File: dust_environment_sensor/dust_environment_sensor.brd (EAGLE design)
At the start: 60 x 34 mm, 4 parts, among them U1 LTP5901, U2 LIS3DH, U3 SI7005, U4 TSL2560

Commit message: Battery holder
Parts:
- added J1: (no value), Cool_Electricity:BX0036
- moved U1 14.1 mm to (30.5, 15.5), turned to 180 degrees
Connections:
- net GND: now also J1.NEG
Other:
- board size 60 x 34 mm -> 60 x 35 mm
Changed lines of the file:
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@@
 <board>
 <plain>
-<wire x1="0" y1="0" x2="60" y2="0" width="0" layer="20"/>
-<wire x1="60" y1="0" x2="60" y2="34" width="0" layer="20"/>
+<wire x1="0" y1="-1" x2="60" y2="-1" width="0" layer="20"/>
+<wire x1="60" y1="-1" x2="60" y2="34" width="0" layer="20"/>
 <wire x1="60" y1="34" x2="0" y2="34" width="0" layer="20"/>
-<wire x1="0" y1="34" x2="0" y2="0" width="0" layer="20"/>
+<wire x1="0" y1="34" x2="0" y2="-1" width="0" layer="20"/>
 </plain>
 <attributes>
@@
 </autorouter>
 <elements>
-<element name="U1" library="Cool_Electricity" package="LTP5901_MODULE" value="LTP5901" x="16.51" y="17.51" rot="R90"/>
+<element name="U1" library="Cool_Electricity" package="LTP5901_MODULE" value="LTP5901" x="30.49" y="15.51" rot="R180"/>
 <element name="U2" library="Cool_Electricity" package="LGA16_ST" value="LIS3DH" x="43.18" y="19.05"/>
 <element name="U3" library="Cool_Electricity" package="QFN24_SILICON_LABS" value="SI7005" x="41.91" y="27.94" rot="R90"/>
 <element name="U4" library="Cool_Electricity" package="CL6_TAOS" value="TSL2560" x="45.72" y="11.43"/>
+<element name="J1" library="Cool_Electricity" package="BX0036" value="" x="30" y="17" rot="MR0"/>
 </elements>
 <signals>
@@
 <contactref element="U2" pad="12"/>
 <contactref element="U2" pad="10"/>
-<wire x1="22.01" y1="5.51" x2="32.01" y2="5.51" width="0" layer="19" extent="1-1"/>
-<wire x1="13.01" y1="5.51" x2="22.01" y2="5.51" width="0" layer="19" extent="1-1"/>
-<wire x1="3.01" y1="5.51" x2="13.01" y2="5.51" width="0" layer="19" extent="1-1"/>
-<wire x1="33.01" y1="21.51" x2="32.01" y2="5.51" width="0" layer="19" extent="1-1"/>
-<wire x1="32.01" y1="29.51" x2="33.01" y2="21.51" width="0" layer="19" extent="1-1"/>
-<wire x1="27.01" y1="29.51" x2="32.01" y2="29.51" width="0" layer="19" extent="1-1"/>
-<wire x1="13.01" y1="29.51" x2="27.01" y2="29.51" width="0" layer="19" extent="1-1"/>
-<wire x1="3.01" y1="29.51" x2="13.01" y2="29.51" width="0" layer="19" extent="1-1"/>
-<wire x1="44.035" y1="28.69" x2="3.01" y2="29.51" width="0" layer="19" extent="1-1"/>
+<contactref element="J1" pad="NEG"/>
 <wire x1="44.035" y1="27.19" x2="44.035" y2="28.69" width="0" layer="19" extent="1-1"/>
 <wire x1="41.91" y1="27.94" x2="44.035" y2="28.69" width="0" layer="19" extent="1-1"/>
+<wire x1="40.66" y1="25.815" x2="41.91" y2="27.94" width="0" layer="19" extent="1-1"/>
 <wire x1="39.785" y1="29.19" x2="41.91" y2="27.94" width="0" layer="19" extent="1-1"/>
-<wire x1="40.66" y1="25.815" x2="41.91" y2="27.94" width="0" layer="19" extent="1-1"/>
 <wire x1="44.73" y1="19.55" x2="40.66" y2="25.815" width="0" layer="19" extent="1-1"/>
 <wire x1="44.73" y1="18.55" x2="44.73" y2="19.55" width="0" layer="19" extent="1-1"/>
 <wire x1="41.63" y1="18.05" x2="44.73" y2="18.55" width="0" layer="19" extent="1-1"/>
+<wire x1="18.49" y1="31.01" x2="39.785" y2="29.19" width="0" layer="19" extent="1-1"/>
+<wire x1="18.49" y1="26.01" x2="18.49" y2="31.01" width="0" layer="19" extent="1-1"/>
+<wire x1="26.49" y1="32.01" x2="18.49" y2="31.01" width="0" layer="19" extent="1-1"/>
+<wire x1="18.49" y1="12.01" x2="18.49" y2="26.01" width="0" layer="19" extent="1-1"/>
+<wire x1="18.49" y1="2.01" x2="18.49" y2="12.01" width="0" layer="19" extent="1-1"/>
+<wire x1="42.49" y1="31.01" x2="41.63" y2="18.05" width="0" layer="19" extent="1-1"/>
+<wire x1="42.49" y1="21.01" x2="42.49" y2="31.01" width="0" layer="19" extent="1-1"/>
+<wire x1="42.49" y1="12.01" x2="42.49" y2="21.01" width="0" layer="19" extent="1-1"/>
+<wire x1="42.49" y1="2.01" x2="42.49" y2="12.01" width="0" layer="19" extent="1-1"/>
+<wire x1="2.2" y1="17" x2="42.49" y2="31.01" width="0" layer="19" extent="1-1"/>
 </signal>
 </signals>

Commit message: more work on dust sensor
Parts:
- added C1, C3, C5: 100n, rcl:C0603
- added C2: 10u, rcl:C0603
- added C31, C32: 22p, SparkFun:0603
- added C33, C34, C41: .1u, SparkFun:0603
- added C4: 100u, rcl:C0603
- added C6: (no value), rcl:C0603
- added C7: 4.7u, rcl:C0603
- added JP1: (no value), custom:1X06
- added JP2: AVR_SPI_PRG_6NS, SparkFun:2X3-NS
- added R1, R2: 2.2k, resistor:R0603
- added R46: 10k, SparkFun:0603
- added U5: ATMEGA168, SparkFun:TQFP32-08
- added X1: 32.768KHz, WSNlib:ABS07
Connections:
- new net 5V: C33.2, C34.2, JP1.3, JP2.2, R46.2, U5.18, U5.4, U5.6
- new net ACCEL_INT1: U2.11
- new net ACCEL_INT2: U2.9
- new net ATMEGA_TO_MOTE: JP1.5, U1.59, U5.31
- new net HUMID_#CS: U3.15
- new net I2C_SCL: R1.1, U2.4, U3.3, U4.4, U5.28
- new net I2C_SDA: R2.1, U2.6, U3.4, U4.5, U5.27
- new net LIGHT_INT: U4.6
- new net MISO: JP2.1, U5.16
- new net MOSI: JP2.4, U5.15
- new net MOTE_TO_ATMEGA: JP1.4, U1.62, U5.30
- new net N$1: C7.1, U3.10
- new net N$2: C31.1, U5.7, X1.2
- new net N$4: C32.1, U5.8, X1.1
- new net RST: C41.1, JP2.5, R46.1, U5.29
- new net RTS#: C41.2, JP1.6
- new net SCLK: JP2.3, U5.17
- new net VCC: C1.1, C2.1, C3.1, C4.1, C5.1, C6.1, J1.POS, R1.2, R2.2, U1.55, U2.14, U2.7, U2.8, U3.9, U4.1
- net GND: now also C1.2, C2.2, C3.2, C31.2, C32.2, C33.1, C34.1, C4.2, C5.2, C6.2, C7.2, JP1.1, JP1.2, JP2.6, U4.2, U5.21, U5.3, U5.5

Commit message: BOM done
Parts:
- added JP3: .1" header, con-lstb:MA06-2
- added LED1: RED, led:CHIPLED_0805
- added R3: 15, resistor:R0603
- added R4: 120, SparkFun:0603
- added STANDOFF1, STANDOFF2, STANDOFF3, STANDOFF4: STAND-OFF, SparkFun-Electromechanical:STAND-OFF
- C4: device rcl:C0603 -> SparkFun-Capacitors:EIA3216-KIT
- C6: value (none) -> 100n
- J1: value (none) -> 3.6V Lithium C cell
- JP1: value (none) -> 87758-1016; device custom:1X06 -> con-molex:87758-1016
- U5: value ATMEGA168 -> ATMEGA328P
- moved JP2 156.6 mm to (50.0, 60.0), flipped to the bottom, turned to 270 degrees
- moved JP1 155.0 mm to (27.0, 54.0), turned to 180 degrees
- moved C41 146.1 mm to (32.0, 66.0), turned to 90 degrees
- moved R46 143.9 mm to (29.0, 65.0), turned to 180 degrees
- moved C34 141.8 mm to (42.0, 65.0)
- moved X1 139.2 mm to (44.0, 51.0), turned to 180 degrees
- moved C33 128.8 mm to (41.0, 51.0), turned to 90 degrees
- moved C31 128.7 mm to (43.0, 48.0), turned to 270 degrees
- moved C32 128.4 mm to (46.0, 48.0), turned to 270 degrees
- moved U5 118.3 mm to (41.0, 58.0), turned to 90 degrees
- moved R2 111.4 mm to (53.0, 53.0), turned to 90 degrees
- moved R1 106.9 mm to (50.9, 53.0), turned to 90 degrees
- moved C2 89.2 mm to (62.0, 49.0)
- moved C5 85.0 mm to (59.0, 34.0)
- moved C1 84.3 mm to (58.0, 50.0)
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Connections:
- removed net 5V: C33.2, C34.2, JP1.3, JP2.2, R46.2, U5.18, U5.4, U5.6
- removed net ATMEGA_TO_MOTE: JP1.5, U1.59, U5.31
- removed net HUMID_#CS: U3.15
- removed net MOTE_TO_ATMEGA: JP1.4, U1.62, U5.30
- new net ATMEGA_RX: JP3.7, U5.30
- new net ATMEGA_TX: JP3.9, U5.31
- new net FLASH_P_ENN: JP1.2, U1.51
- new net HUMID_VCC: R3.2, U5.25
- new net IPCS_MISO: JP1.5, U1.33
- new net IPCS_MOSI: JP1.4, U1.35
- new net IPCS_SCK: JP1.3, U1.36
- new net IPCS_SSN: JP1.1, U1.39
- new net LED1: R4.2, U5.26
- new net MOTE_API_RX: JP3.10, U1.59
- new net MOTE_API_TX: JP3.8, U1.62
- new net MOTE_CLI_RX: JP1.10, U1.32
- new net MOTE_CLI_TX: JP1.9, U1.31
- new net MOTE_RADIO_INHIBIT: U1.64, U5.12
- new net MOTE_RESETN: JP1.6, U1.15, U5.11
- new net MOTE_RX_CTSN: U1.58, U5.10
- new net MOTE_RX_RTSN: U1.57, U5.9
- new net MOTE_SLEEPN: U1.27, U5.13
- new net MOTE_TIMEN: U1.63, U5.14
- new net MOTE_TX_CTSN: U1.61, U5.2
- new net MOTE_TX_RTSN: U1.60, U5.1
- new net N$3: C5.1, R3.1, U3.9
- new net N$5: LED1.A, R4.1
- new net VBATT: C4.A, J1.POS, JP3.4
- net ACCEL_INT1: now also U5.32
- net ACCEL_INT2: now also U5.23
- net GND: now also C4.C, JP1.8, JP3.1, JP3.3, LED1.C, U3.15, U5.19, U5.22; no longer C4.2, JP1.1, JP1.2
- net LIGHT_INT: now also U5.24
- net RTS#: now also JP3.11; no longer JP1.6
- net VCC: now also C33.2, C34.2, JP1.7, JP2.2, JP3.6, R46.2, U5.18, U5.4, U5.6; no longer C4.1, C5.1, J1.POS, U3.9
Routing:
- net GND: track 0.00 -> 272.6 mm, vias 0 -> 1
- net VCC: track 0.00 -> 192.7 mm, vias 0 -> 2
- net MOTE_RADIO_INHIBIT: track 0.00 -> 95.4 mm, vias 0 -> 2
- net MOTE_TIMEN: track 0.00 -> 89.9 mm, vias 0 -> 2
- net I2C_SDA: track 0.00 -> 69.6 mm, vias 0 -> 5
- net MOTE_API_TX: track 0.00 -> 68.1 mm, vias 0 -> 1
- net HUMID_VCC: track 0.00 -> 67.0 mm, vias 0 -> 2
- net MOTE_RESETN: track 0.00 -> 62.2 mm, vias 0 -> 2
- net FLASH_P_ENN: track 0.00 -> 59.5 mm
- net LIGHT_INT: track 0.00 -> 55.6 mm, vias 0 -> 2
- net MOTE_API_RX: track 0.00 -> 55.0 mm, vias 0 -> 2
- net I2C_SCL: track 0.00 -> 52.0 mm, vias 0 -> 5
- net MOTE_RX_RTSN: track 0.00 -> 50.6 mm, vias 0 -> 4
- net MOTE_RX_CTSN: track 0.00 -> 47.5 mm, vias 0 -> 4
- net MOTE_TX_CTSN: track 0.00 -> 44.2 mm, vias 0 -> 2
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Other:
- board size 60 x 35 mm -> 70.8 x 68.7 mm

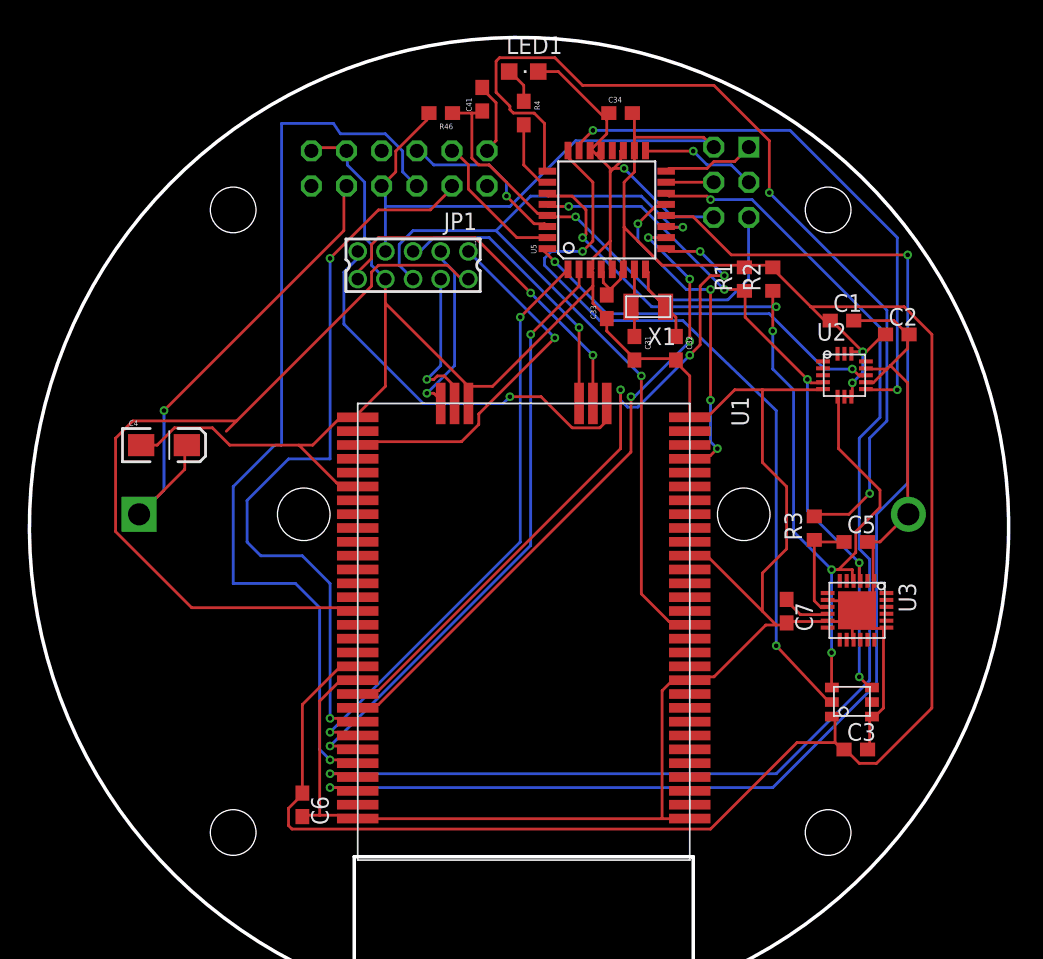
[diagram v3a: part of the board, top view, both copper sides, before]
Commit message: Added new version of power strip
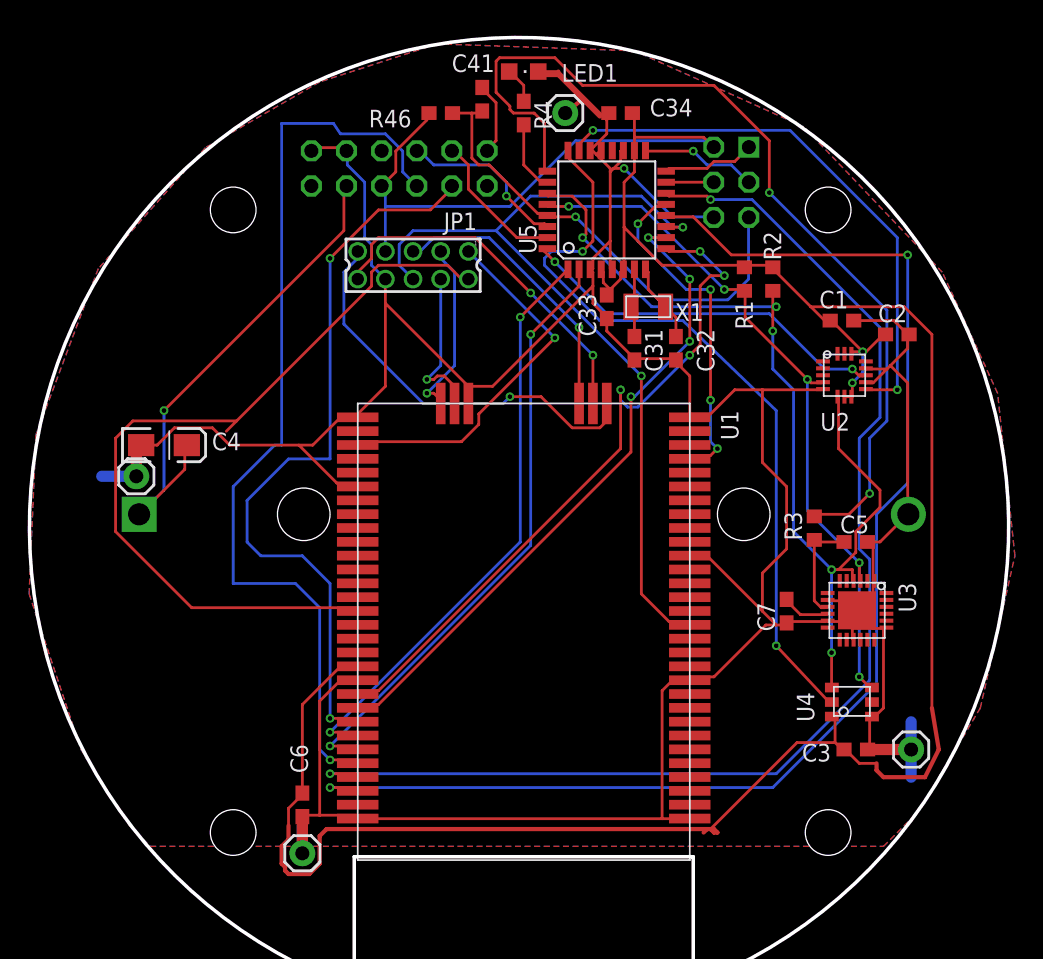
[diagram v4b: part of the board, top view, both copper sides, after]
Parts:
- added JP4, JP5, JP6, JP7: M01PTH, SparkFun-Connectors:1X01
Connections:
- net GND: now also JP4.1, JP5.1, JP6.1, JP7.1
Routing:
- net GND: track 272.6 -> 296.7 mm
- net VCC: track 192.7 -> 204.4 mm
- added copper zone on layer 16, net GND
- added copper zone on layer 1, net VCC
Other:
- board text added: "NEGATIVE"
- board text added: "POSITIVE"
- board text added: "U4"

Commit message: Latest Powerstrip changes
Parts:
- removed C31, C32: 22p, SparkFun:0603
- removed C33, C34, C41: .1u, SparkFun:0603
- removed JP2: AVR_SPI_PRG_6NS, SparkFun:2X3-NS
- removed JP3: .1" header, con-lstb:MA06-2
- removed LED1: RED, led:CHIPLED_0805
- removed R46: 10k, SparkFun:0603
- removed X1: 32.768KHz, WSNlib:ABS07
- added C10, C13, C15, C8, C9: 100n, rcl:C0603
- added C11, C12: TODO, rcl:C0603
- added C14: 10u, rcl:C0603
- added IC2: ATMEGA644A, atmel:TQFP44
- added J2: EXP, SparkFun-Connectors:2X3
- added J3: XBEE_1-10SMT, Cool_Electricity:XBEE_1-10_SMT
- added J4: XBEE_11-20SMT, Cool_Electricity:XBEE_11-20_SMT
- added JP8: (no value), custom:1X06
- added JP9: JTAG, SparkFun-Connectors:AVR_ICSP
- added LED2, LED3: (no value), led:CHIPLED_0805
- added R5: 0R, resistor:R0603
- added U6: L3GD20, Cool_Electricity:LGA16_4X4_ST
- added X2: 32.768KHz, WSNlib:ABS07
- R4: value 120 -> 10k; device SparkFun:0603 -> resistor:R0603
- U5: value ATMEGA328P -> AMN41121; device SparkFun:TQFP32-08 -> Cool_Electricity:AMN41121
- moved JP7 56.1 mm to (9.00, 17.0)
- moved C1 49.0 mm to (12.9, 30.9), turned to 270 degrees
- moved C6 47.1 mm to (64.0, 29.0)
- moved R4 45.2 mm to (9.75, 27.5)
- moved U5 19.2 mm to (22.0, 61.0), turned to 0 degrees
- moved JP6 8.00 mm to (7.00, 46.8)
- moved JP1 7.21 mm to (23.0, 48.0)
- moved C5 5.10 mm to (54.0, 33.0), turned to 90 degrees
- moved JP5 3.57 mm to (18.7, 7.94)
- moved C4 1.00 mm to (9.00, 42.0)
- moved R3 0.10 mm to (56.1, 35.0)
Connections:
- removed net ATMEGA_RX: JP3.7, U5.30
- removed net ATMEGA_TX: JP3.9, U5.31
- removed net MISO: JP2.1, U5.16
- removed net MOSI: JP2.4, U5.15
- removed net N$4: C32.1, U5.8, X1.1
- removed net N$5: LED1.A, R4.1
- removed net SCLK: JP2.3, U5.17
- new net ATMEGA_TO_FTDI: IC2.10, JP8.5
- new net EXP_CSN: IC2.44, J2.5
- new net EXP_MISO: IC2.2, J2.1
- new net EXP_MOSI: IC2.1, J2.4
- new net EXP_SCK: IC2.3, J2.3
- new net FTDI_TO_ATMEGA: IC2.9, JP8.4
- new net GYRO_INT2: IC2.43, U6.6
- new net LED2: IC2.13, LED3.A
- new net N$6: C11.1, IC2.25, X2.2
- new net N$7: C12.1, IC2.26, X2.1
- new net PIR_OUT: IC2.16, U5.OUT
- new net PIR_VCC: IC2.30, U5.VDD
- new net TCK: IC2.21, JP9.1
- new net TDI: IC2.24, JP9.9
- new net TDO: IC2.23, JP9.3
- new net TMS: IC2.22, JP9.5
- net ACCEL_INT1: now also IC2.37; no longer U5.32
- net ACCEL_INT2: now also IC2.36; no longer U5.23
- net GND: now also C11.2, C12.2, C13.2, C14.2, C15.2, C8.1, C9.1, IC2.18, IC2.28, IC2.39, IC2.6, J2.6, J3.10, JP8.1, JP8.2, JP9.10, JP9.2, LED2.C, LED3.C, U5.GND, U6.10, U6.11, U6.12, U6.13, U6.8, U6.9; no longer C31.2, C32.2, C33.1, C34.1, JP2.6, JP3.1, JP3.3, LED1.C, U5.19, U5.21, U5.22, U5.3, U5.5
- net HUMID_VCC: now also IC2.35; no longer U5.25
- net I2C_SCL: now also IC2.19, U6.2; no longer U5.28
- net I2C_SDA: now also IC2.20, U6.3; no longer U5.27
- net LED1: now also IC2.14, LED2.A; no longer R4.2, U5.26
- net LIGHT_INT: now also IC2.31; no longer U5.24
- net MOTE_API_RX: now also IC2.12, J3.3; no longer JP3.10
- net MOTE_API_TX: now also IC2.11, J3.2; no longer JP3.8
- net MOTE_RADIO_INHIBIT: now also IC2.32; no longer U5.12
- net MOTE_RESETN: now also J3.5; no longer U5.11
- net MOTE_RX_CTSN: now also IC2.40; no longer U5.10
- net MOTE_RX_RTSN: now also IC2.15, J4.16; no longer U5.9
- net MOTE_SLEEPN: now also IC2.33, J3.9; no longer U5.13
- net MOTE_TIMEN: now also IC2.34; no longer U5.14
- net MOTE_TX_CTSN: now also IC2.41; no longer U5.2
- net MOTE_TX_RTSN: now also IC2.42; no longer U5.1
- net N$2: now also C15.1, U6.14; no longer C31.1, U5.7, X1.2
- net RST: now also C10.1, IC2.4, JP9.6, R4.1; no longer C41.1, JP2.5, R46.1, U5.29
- net RTS#: now also C10.2, JP8.6; no longer C41.2, JP3.11
- net VBATT: now also R5.2; no longer JP3.4
- net VCC: now also C13.1, C14.1, C8.2, C9.2, IC2.17, IC2.27, IC2.38, IC2.5, J2.2, J3.1, JP9.4, R4.2, R5.1, U6.1, U6.15, U6.16, U6.4, U6.5; no longer C33.2, C34.2, JP2.2, JP3.6, R46.2, U5.18, U5.4, U5.6
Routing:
- net VCC: track 204.4 -> 83.8 mm, vias 2 -> 9
- net MOTE_SLEEPN: track 24.8 -> 120.7 mm, vias 4 -> 3
- net GND: track 296.7 -> 231.7 mm, vias 1 -> 10
- net ATMEGA_TO_FTDI: track 0.00 -> 59.1 mm, vias 0 -> 4
- net FTDI_TO_ATMEGA: track 0.00 -> 52.3 mm, vias 0 -> 1
- net EXP_CSN: track 0.00 -> 36.5 mm, vias 0 -> 3
- net GYRO_INT2: track 0.00 -> 35.4 mm, vias 0 -> 3
- net I2C_SCL: track 52.0 -> 87.1 mm
- net FLASH_P_ENN: track 59.5 -> 28.0 mm, vias 0 -> 1
- net RST: track 34.9 -> 66.3 mm, vias 1 -> 3
- net HUMID_VCC: track 67.0 -> 38.9 mm
- net EXP_SCK: track 0.00 -> 26.9 mm, vias 0 -> 1
- net VBATT: track 36.5 -> 10.7 mm, vias 1 -> 0
- net PIR_OUT: track 0.00 -> 25.6 mm, vias 0 -> 1
- net MOTE_TIMEN: track 89.9 -> 64.9 mm
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- added copper zone on layer 15, net GND
- added copper zone on layer 2, net VCC
- removed copper zone on layer 16, net GND
- removed copper zone on layer 1, net VCC
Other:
- board text added: "COVER BEFORE SOLDERING DUST MOTE"
- board text added: "Dust Sensor PCB Kevin Weekly"
- board text added: "EXP"
- board text added: "FTDI"
- board text added: "JTAG"

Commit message: BOM Updates
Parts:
- C11, C12: value TODO -> 10p
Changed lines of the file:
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@@
 <attribute name="VALUE" x="34.746" y="69.794" size="0.4064" layer="27" font="vector"/>
 </element>
-<element name="C11" library="rcl" package="C0603" value="TODO" x="41.5" y="63" smashed="yes">
+<element name="C11" library="rcl" package="C0603" value="10p" x="41.5" y="63" smashed="yes">
 <attribute name="NAME" x="42.389" y="63.889" size="1.778" layer="25"/>
 <attribute name="VALUE" x="40.865" y="61.095" size="1.27" layer="27"/>
 </element>
-<element name="C12" library="rcl" package="C0603" value="TODO" x="34" y="63" smashed="yes" rot="R180">
+<element name="C12" library="rcl" package="C0603" value="10p" x="34" y="63" smashed="yes" rot="R180">
 <attribute name="NAME" x="31.841" y="63.635" size="1.778" layer="25" rot="R180"/>
 <attribute name="VALUE" x="34.635" y="64.905" size="1.27" layer="27" rot="R180"/>
